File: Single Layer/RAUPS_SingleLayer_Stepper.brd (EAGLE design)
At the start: 71.4 x 68.6 mm, 30 parts

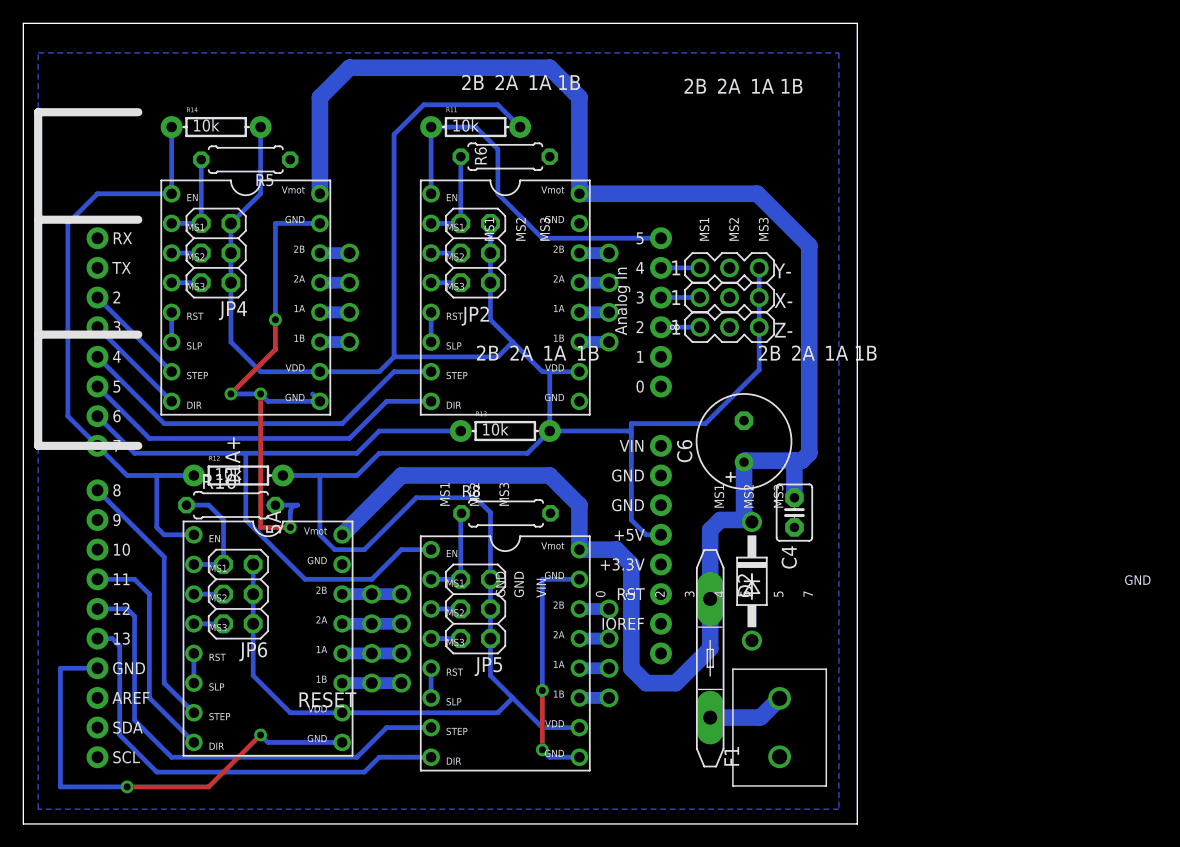
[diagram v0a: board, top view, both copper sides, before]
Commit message: Added BOM, final single layer board tweaks, and re-organized file structure to better reflect project goals
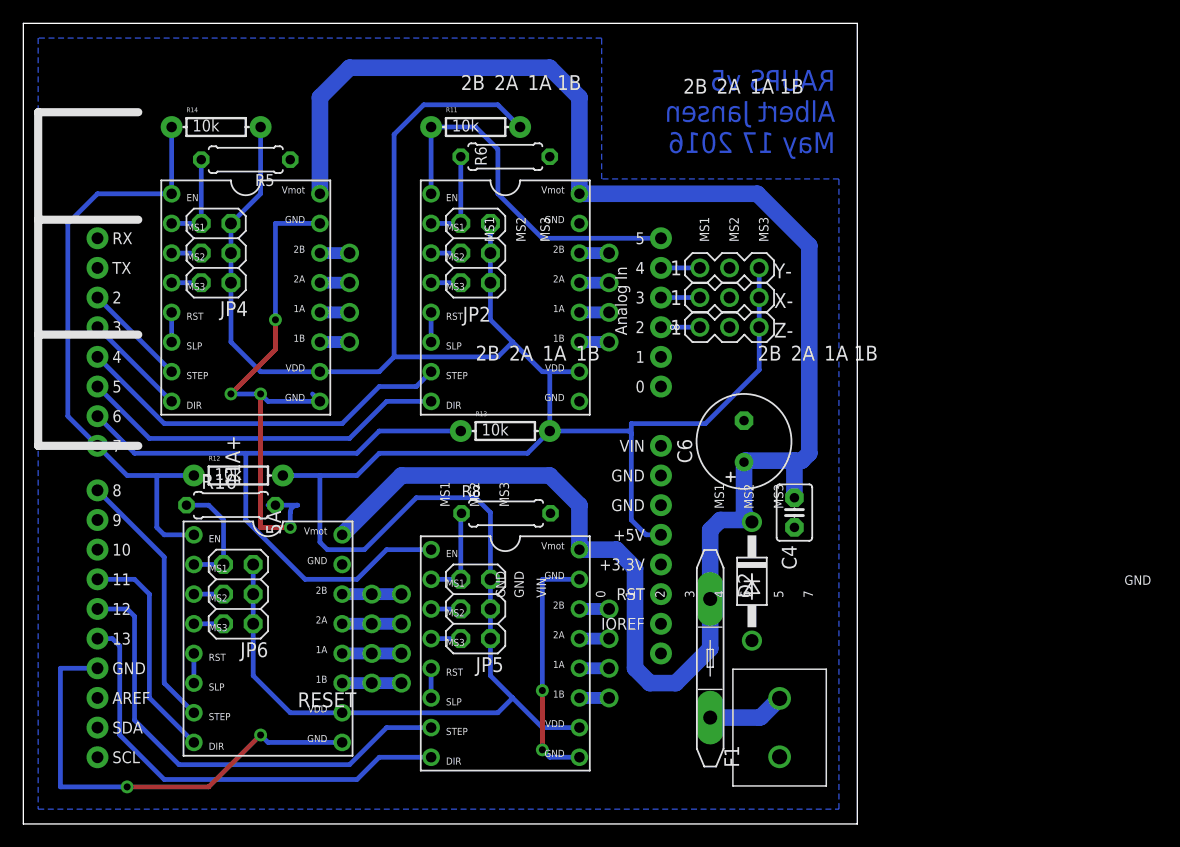
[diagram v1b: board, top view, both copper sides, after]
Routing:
- net Y-STEP: track 40.1 -> 40.6 mm
- net Y-DIR: track 38.3 -> 38.8 mm
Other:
- board text added: "RAUPS v5 Albert Jansen May 17 2016"
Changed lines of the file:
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@@
 <setting verticaltext="up"/>
 </settings>
-<grid distance="50" unitdist="mil" unit="mil" style="lines" multiple="1" display="yes" altdistance="25" altunitdist="mil" altunit="mil"/>
+<grid distance="50" unitdist="mil" unit="mil" style="lines" multiple="1" display="yes" altdistance="12.5" altunitdist="mil" altunit="mil"/>
 <layers>
 <layer number="1" name="Top" color="4" fill="1" visible="yes" active="yes"/>
@@
 <text x="-8.89" y="33.655" size="1.4224" layer="48">+</text>
 <text x="-16.51" y="60.96" size="1.4224" layer="48">12-35V Out</text>
+<text x="69.5325" y="57.4675" size="1.778" layer="16" font="vector" rot="MR0">RAUPS v5
+Albert Jansen
+May 17 2016</text>
 </plain>
 <attributes>
@@
 <contactref element="D2" pad="A"/>
 <contactref element="U$8" pad="GND@0"/>
-<polygon width="0.4064" layer="16" isolate="0.8128">
-<vertex x="1.27" y="66.04"/>
-<vertex x="69.85" y="66.04"/>
-<vertex x="69.85" y="1.27"/>
-<vertex x="1.27" y="1.27"/>
-</polygon>
 <contactref element="U$1" pad="P$2"/>
 <wire x1="21.59" y1="27.305" x2="20.955" y2="27.305" width="0.4064" layer="16"/>
@@
 <wire x1="22.86" y1="25.4" x2="20.32" y2="25.4" width="0.4064" layer="1"/>
 <wire x1="20.32" y1="25.4" x2="20.32" y2="36.83" width="0.4064" layer="1"/>
+<polygon width="0.6096" layer="16">
+<vertex x="1.27" y="1.27"/>
+<vertex x="69.85" y="1.27"/>
+<vertex x="69.85" y="55.245"/>
+<vertex x="49.53" y="55.245"/>
+<vertex x="49.53" y="67.31"/>
+<vertex x="1.27" y="67.31"/>
+</polygon>
 </signal>
 <signal name="N$6">
@@
 <wire x1="17.78" y1="51.435" x2="20.32" y2="53.975" width="0.4064" layer="16"/>
 <wire x1="20.32" y1="53.975" x2="20.32" y2="59.69" width="0.4064" layer="16"/>
-<wire x1="25.4" y1="29.845" x2="28.575" y2="29.845" width="0.4064" layer="16"/>
 <wire x1="19.685" y1="22.225" x2="19.685" y2="19.685" width="0.4064" layer="16"/>
 <wire x1="22.225" y1="29.845" x2="25.4" y2="29.845" width="0.4064" layer="16"/>
-<wire x1="25.4" y1="29.845" x2="25.4" y2="24.765" width="0.4064" layer="16"/>
-<wire x1="25.4" y1="24.765" x2="26.67" y2="23.495" width="0.4064" layer="16"/>
-<wire x1="26.67" y1="23.495" x2="29.21" y2="23.495" width="0.4064" layer="16"/>
+<wire x1="25.4" y1="29.845" x2="28.575" y2="29.845" width="0.4064" layer="16"/>
+<wire x1="26.035" y1="23.495" x2="29.21" y2="23.495" width="0.4064" layer="16"/>
 <wire x1="29.21" y1="23.495" x2="33.655" y2="27.94" width="0.4064" layer="16"/>
 <wire x1="33.655" y1="27.94" x2="38.735" y2="27.94" width="0.4064" layer="16"/>
@@
 <wire x1="58.42" y1="34.29" x2="63.0238" y2="38.8938" width="0.4064" layer="16"/>
 <wire x1="63.0238" y1="38.8938" x2="63.0238" y2="42.545" width="0.4064" layer="16"/>
+<wire x1="26.035" y1="23.495" x2="25.4" y2="24.13" width="0.4064" layer="16"/>
+<wire x1="25.4" y1="24.13" x2="25.4" y2="29.845" width="0.4064" layer="16"/>
 </signal>
 <signal name="N$19">
@@
 <wire x1="47.625" y1="27.305" x2="47.625" y2="23.495" width="1.4224" layer="16"/>
 <wire x1="47.625" y1="23.495" x2="50.8" y2="23.495" width="1.4224" layer="16"/>
-<wire x1="50.8" y1="23.495" x2="52.07" y2="22.225" width="1.4224" layer="16"/>
+<wire x1="50.8" y1="23.495" x2="52.3875" y2="21.9075" width="1.4224" layer="16"/>
 <wire x1="25.4" y1="53.9749" x2="25.4" y2="62.23" width="1.4224" layer="16"/>
 <wire x1="25.4" y1="62.23" x2="27.94" y2="64.77" width="1.4224" layer="16"/>
@@
 <wire x1="47.625" y1="62.23" x2="47.625" y2="53.975" width="1.4224" layer="16"/>
 <wire x1="47.625" y1="53.975" x2="62.865" y2="53.975" width="1.4224" layer="16"/>
-<wire x1="52.07" y1="13.335" x2="53.34" y2="12.065" width="1.4224" layer="16"/>
-<wire x1="53.34" y1="12.065" x2="55.88" y2="12.065" width="1.4224" layer="16"/>
 <wire x1="55.88" y1="12.065" x2="58.8258125" y2="15.0108125" width="1.4224" layer="16"/>
 <wire x1="58.8258125" y1="15.0108125" x2="58.8258125" y2="19.2711625" width="1.4224" layer="16"/>
@@
 <wire x1="45.085" y1="29.845" x2="47.625" y2="27.305" width="1.4224" layer="16"/>
 <wire x1="32.385" y1="29.845" x2="45.085" y2="29.845" width="1.4224" layer="16"/>
-<wire x1="52.07" y1="22.225" x2="52.07" y2="13.335" width="1.4224" layer="16"/>
 <wire x1="62.865" y1="53.975" x2="67.31" y2="49.53" width="1.4224" layer="16"/>
 <wire x1="67.31" y1="49.53" x2="67.31" y2="31.75" width="1.4224" layer="16"/>
 <wire x1="67.31" y1="31.75" x2="66.675" y2="31.115" width="1.4224" layer="16"/>
 <wire x1="66.04" y1="27.94" x2="66.04" y2="31.115" width="1.4224" layer="16"/>
+<wire x1="52.3875" y1="21.9075" x2="52.3875" y2="13.335" width="1.4224" layer="16"/>
+<wire x1="52.3875" y1="13.335" x2="53.6575" y2="12.065" width="1.4224" layer="16"/>
+<wire x1="53.6575" y1="12.065" x2="55.88" y2="12.065" width="1.4224" layer="16"/>
 </signal>
 <signal name="N$17">
@@
 <wire x1="6.35" y1="40.005" x2="12.065" y2="34.29" width="0.4064" layer="16"/>
 <wire x1="12.065" y1="34.29" x2="27.305" y2="34.29" width="0.4064" layer="16"/>
-<wire x1="27.305" y1="34.29" x2="31.75" y2="38.735" width="0.4064" layer="16"/>
-<wire x1="31.75" y1="38.735" x2="34.925" y2="38.735" width="0.4064" layer="16"/>
+<wire x1="27.305" y1="34.29" x2="30.48" y2="37.465" width="0.4064" layer="16"/>
+<wire x1="30.48" y1="37.465" x2="33.655" y2="37.465" width="0.4064" layer="16"/>
+<wire x1="33.655" y1="37.465" x2="34.925" y2="38.735" width="0.4064" layer="16"/>
 </signal>
 <signal name="E0-EN">
@@
 <wire x1="28.575" y1="31.75" x2="30.48" y2="33.655" width="0.4064" layer="16"/>
 <wire x1="30.48" y1="33.655" x2="37.465" y2="33.655" width="0.4064" layer="16"/>
-<wire x1="24.13" y1="20.955" x2="29.845" y2="20.955" width="0.4064" layer="16"/>
 <wire x1="19.05" y1="26.035" x2="19.05" y2="31.75" width="0.4064" layer="16"/>
-<wire x1="29.845" y1="20.955" x2="32.385" y2="23.495" width="0.4064" layer="16"/>
-<wire x1="32.385" y1="23.495" x2="34.925" y2="23.495" width="0.4064" layer="16"/>
+<wire x1="31.115" y1="23.495" x2="34.925" y2="23.495" width="0.4064" layer="16"/>
+<wire x1="24.13" y1="20.955" x2="28.575" y2="20.955" width="0.4064" layer="16"/>
+<wire x1="28.575" y1="20.955" x2="31.115" y2="23.495" width="0.4064" layer="16"/>
 </signal>
 <signal name="Y-STEP">
@@
 <contactref element="U$11" pad="D12"/>
 <wire x1="31.115" y1="8.255" x2="34.925" y2="8.255" width="0.4064" layer="16"/>
-<wire x1="9.525" y1="8.89" x2="12.7" y2="5.715" width="0.4064" layer="16"/>
-<wire x1="28.575" y1="5.715" x2="31.115" y2="8.255" width="0.4064" layer="16"/>
+<wire x1="9.525" y1="8.89" x2="13.335" y2="5.08" width="0.4064" layer="16"/>
+<wire x1="27.94" y1="5.08" x2="31.115" y2="8.255" width="0.4064" layer="16"/>
 <wire x1="6.35" y1="18.415" x2="8.89" y2="18.415" width="0.4064" layer="16"/>
 <wire x1="8.89" y1="18.415" x2="9.525" y2="17.78" width="0.4064" layer="16"/>
 <wire x1="9.525" y1="17.78" x2="9.525" y2="8.89" width="0.4064" layer="16"/>
-<wire x1="12.7" y1="5.715" x2="28.575" y2="5.715" width="0.4064" layer="16"/>
+<wire x1="13.335" y1="5.08" x2="27.94" y2="5.08" width="0.4064" layer="16"/>
 </signal>
 <signal name="Y-DIR">
@@
 <wire x1="6.35" y1="15.875" x2="7.62" y2="15.875" width="0.4064" layer="16"/>
 <wire x1="30.48" y1="5.715" x2="34.925" y2="5.715" width="0.4064" layer="16"/>
-<wire x1="8.255" y1="7.62" x2="11.43" y2="4.445" width="0.4064" layer="16"/>
-<wire x1="29.21" y1="4.445" x2="30.48" y2="5.715" width="0.4064" layer="16"/>
+<wire x1="8.255" y1="7.62" x2="12.065" y2="3.81" width="0.4064" layer="16"/>
+<wire x1="28.575" y1="3.81" x2="30.48" y2="5.715" width="0.4064" layer="16"/>
 <wire x1="7.62" y1="15.875" x2="8.255" y2="15.24" width="0.4064" layer="16"/>
 <wire x1="8.255" y1="15.24" x2="8.255" y2="7.62" width="0.4064" layer="16"/>
-<wire x1="11.43" y1="4.445" x2="29.21" y2="4.445" width="0.4064" layer="16"/>
+<wire x1="28.575" y1="3.81" x2="12.065" y2="3.81" width="0.4064" layer="16"/>
 </signal>
 <signal name="X-MIN">
@@
 </board>
 </drawing>
+<compatibility>
+<note version="6.3" minversion="6.2.2" severity="warning">
+Since Version 6.2.2 text objects can contain more than one line,
+which will not be processed correctly with this version.
+</note>
+</compatibility>
 </eagle>
